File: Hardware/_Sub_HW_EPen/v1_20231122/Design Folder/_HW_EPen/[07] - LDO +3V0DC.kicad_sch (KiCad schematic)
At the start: 4 parts, among them U701 MIC5365-3.0YC5-TR

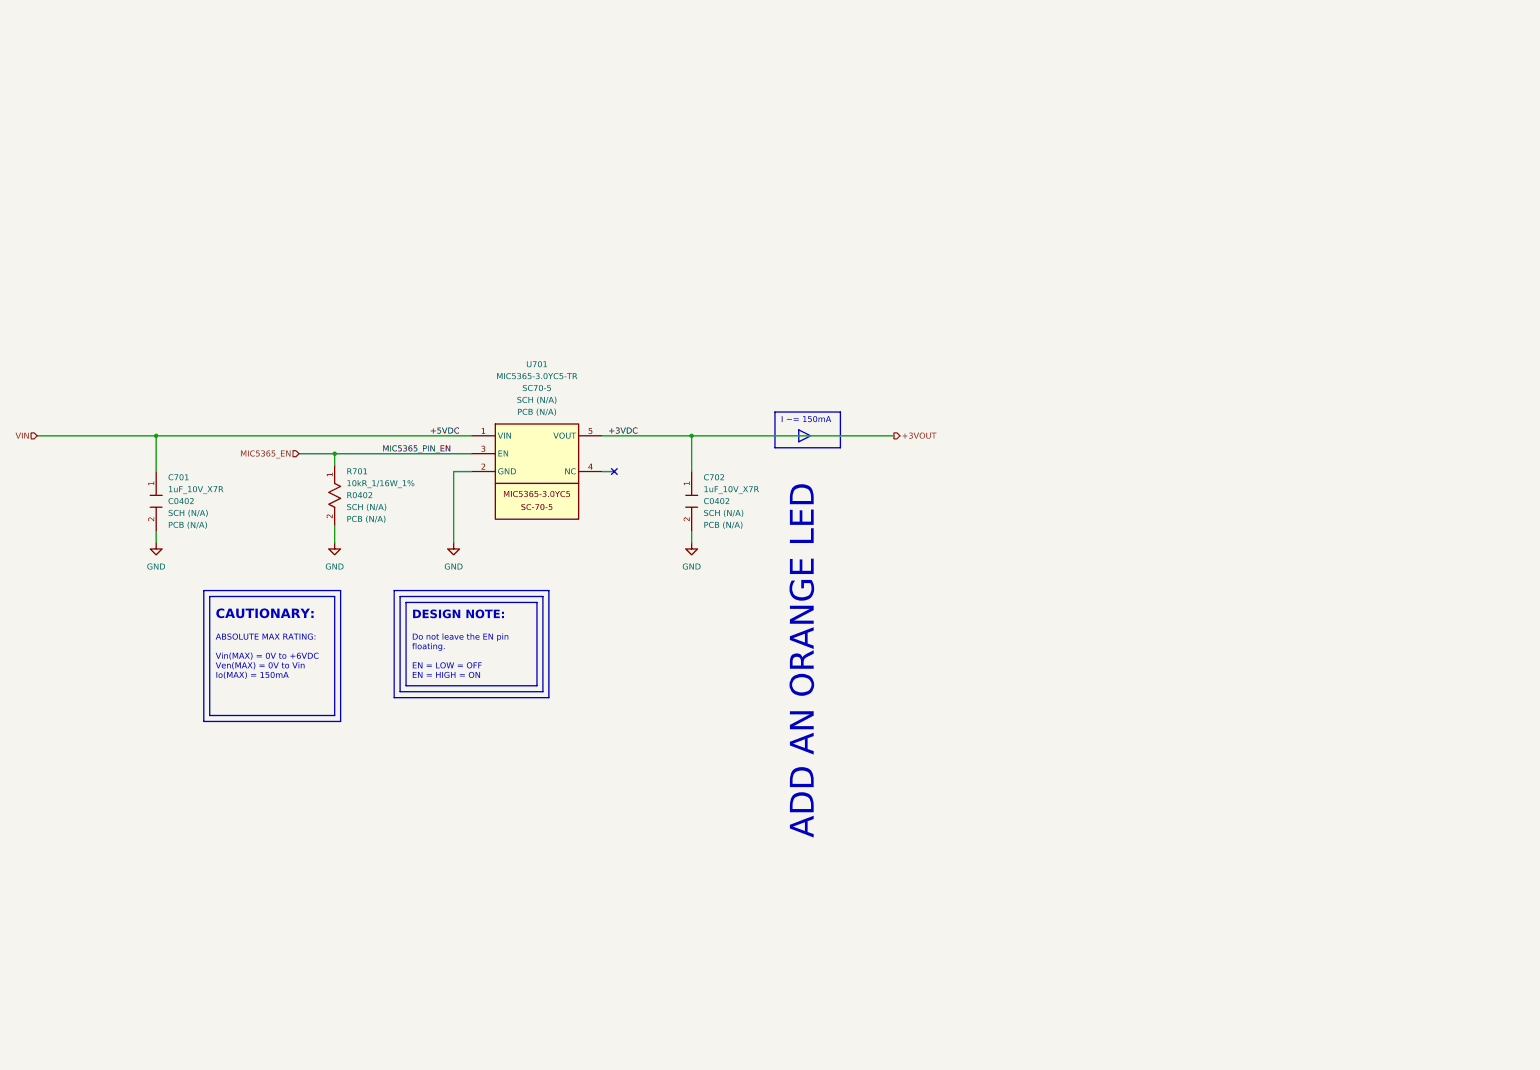
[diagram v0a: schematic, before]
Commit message: Working on EPen schematic
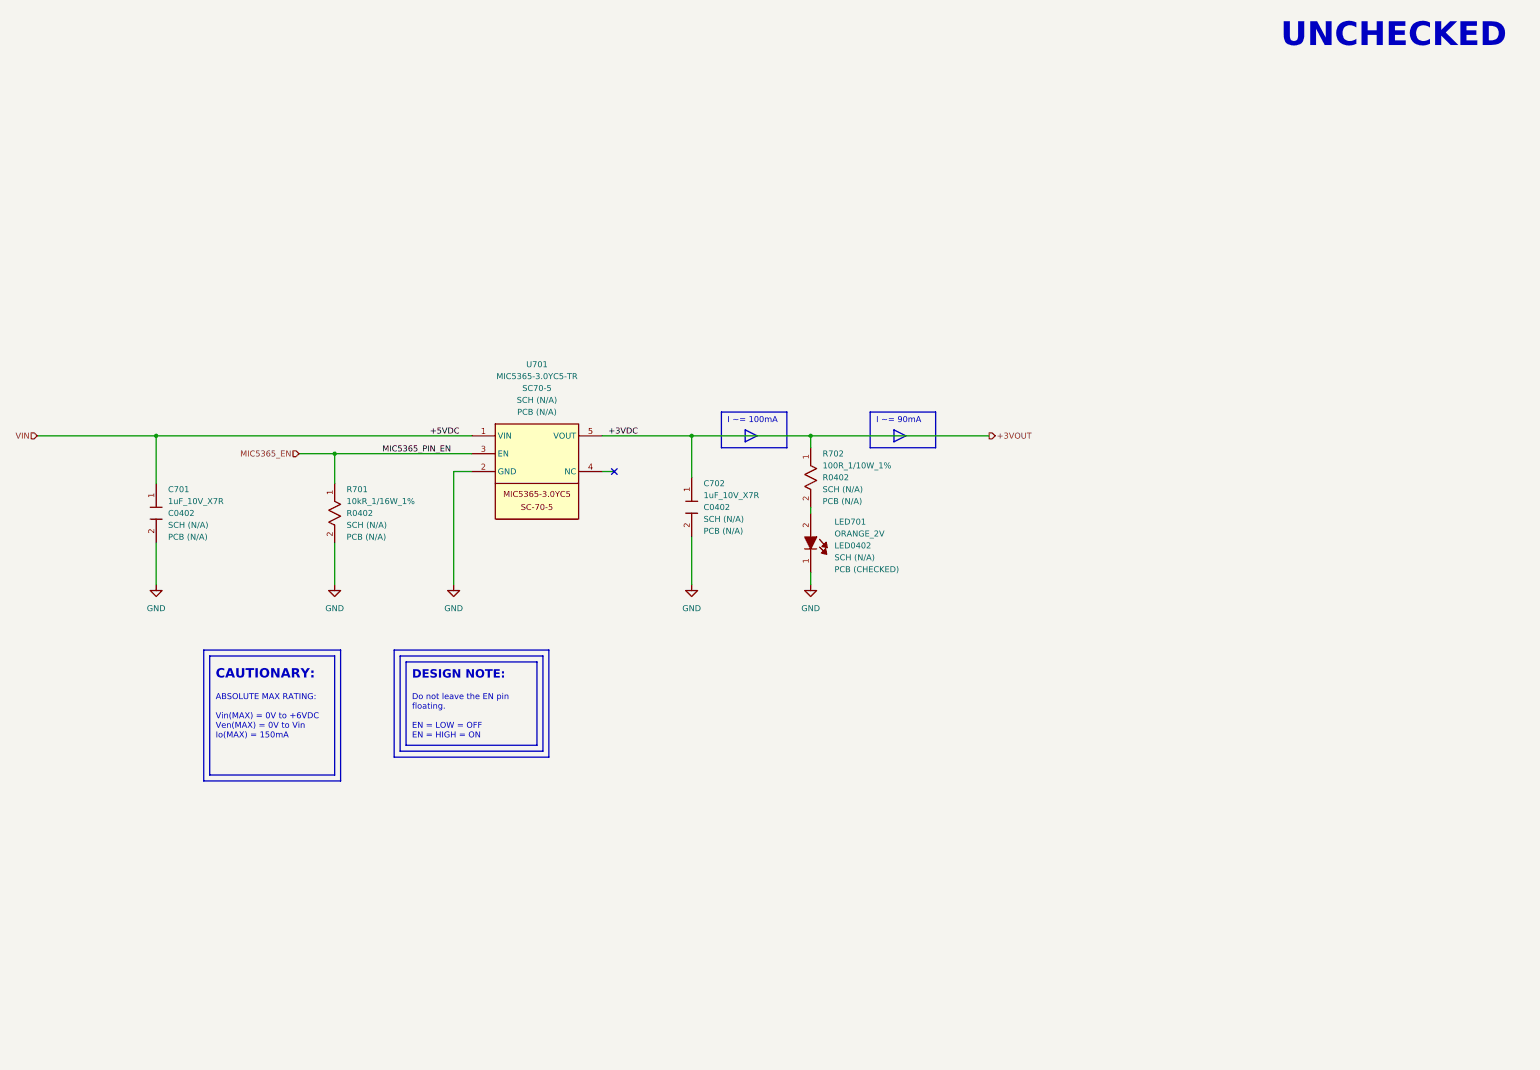
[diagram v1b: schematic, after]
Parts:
- added LED701: ORANGE_2V, LED_SMD:LED_0402_1005Metric, symbol _SCHLIB_EPen:LED_ORANGE_2V_605nm_LED0402
- added R702: 100R_1/10W_1%, Resistor_SMD:R_0402_1005Metric, symbol _SCHLIB_EPen:RES_100R_1/10W_1%_R0402
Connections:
- net +3VOUT: now also R702.1
- net GND: now also LED701.1
- new net: LED701.2, R702.2
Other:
- note added: "I ~= 100mA"
- note added: "I ~= 90mA"
- note added: "UNCHECKED"
- note removed: "ADD AN ORANGE LED"
- note removed: "I ~= 150mA"
- moved on the sheet: C701, C702, R701

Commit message: More progress on EPen Hardware
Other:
- note removed: "UNCHECKED"
- company: (none) -> mend0z0
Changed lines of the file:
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@@
 (kicad_sch (version 20230121) (generator eeschema)
   (paper "B")
+  (title_block
+    (company "mend0z0")
+    (comment 1 "v1.0")
+    (comment 2 "PRELIMINARY")
+    (comment 4 "_BOM_EPen.html")
+    (comment 5 "_HW_EPen.pcb")
+    (comment 6 "_GBR_EPen.zip")
+    (comment 7 "_BOM_EPen.html")
+    (comment 9 "First Release")
+  )
   (junction (at 127 119.38) (diameter 0) (color 0 0 0 0)
   )
@@
     (fill (type none))
   )
-  (text "UNCHECKED" (at 367.03 36.83 0)
-    (effects (font (size 5.08 5.08) (thickness 1.016) bold) (justify left bottom))
-  )
   (text "CAUTIONARY:" (at 139.7 171.45 0)

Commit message: _HW_EPen is ready to be worked for layout
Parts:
- C701, C702, LED701, R701, R702, U701: SCH CHECK SCH (N/A) -> SCH (CHECKED)
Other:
- note added: "Do not leave the EN pin floating. EN = LOW = OFF (default) EN = HIGH = ON"
- note removed: "Do not leave the EN pin floating. EN = LOW = OFF EN = HIGH = ON"
- title: (none) -> _HW_EPen
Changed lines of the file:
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@@
   (paper "B")
   (title_block
+    (title "_HW_EPen")
+    (date "2023-11-28")
+    (rev "v1.0")
     (company "mend0z0")
     (comment 1 "v1.0")
-    (comment 2 "PRELIMINARY")
+    (comment 2 "CHECKED")
     (comment 4 "_BOM_EPen.html")
     (comment 5 "_HW_EPen.pcb")
     (comment 6 "_GBR_EPen.zip")
     (comment 7 "_BOM_EPen.html")
+    (comment 8 "N/A")
     (comment 9 "First Release")
   )
@@
     (effects (font (size 1.27 1.27)) (justify left bottom))
   )
-  (text "Do not leave the EN pin\nfloating.\n\nEN = LOW = OFF\nEN = HIGH = ON"
+  (text "Do not leave the EN pin\nfloating.\n\nEN = LOW = OFF (default)\nEN = HIGH = ON"
     (at 181.61 184.15 0)
     (effects (font (size 1.27 1.27)) (justify left bottom))
@@
       (effects (font (size 1.27 1.27)) (justify left))
     )
-    (property "SCH CHECK" "SCH (N/A)" (at 129.54 138.43 90)
+    (property "SCH CHECK" "SCH (CHECKED)" (at 129.54 138.43 90)
       (effects (font (size 1.27 1.27)) (justify left))
     )
@@
       (effects (font (size 1.27 1.27)) (justify left))
     )
-    (property "SCH CHECK" "SCH (N/A)" (at 269.24 130.81 90)
+    (property "SCH CHECK" "SCH (CHECKED)" (at 269.24 130.81 90)
       (effects (font (size 1.27 1.27)) (justify left))
     )
@@
       (effects (font (size 1.27 1.27)) (justify left))
     )
-    (property "SCH CHECK" "SCH (N/A)" (at 167.64 138.43 90)
+    (property "SCH CHECK" "SCH (CHECKED)" (at 167.64 138.43 90)
       (effects (font (size 1.27 1.27)) (justify left))
     )
@@
       (effects (font (size 1.27 1.27)) (justify left))
     )
-    (property "SCH CHECK" "SCH (N/A)" (at 271.78 145.3515 90)
+    (property "SCH CHECK" "SCH (CHECKED)" (at 271.78 145.3515 90)
       (effects (font (size 1.27 1.27)) (justify left))
     )
@@
       (effects (font (size 1.27 1.27)) (justify left))
     )
-    (property "SCH CHECK" "SCH (N/A)" (at 243.84 137.16 90)
+    (property "SCH CHECK" "SCH (CHECKED)" (at 243.84 137.16 90)
       (effects (font (size 1.27 1.27)) (justify left))
     )
@@
       (effects (font (size 1.27 1.27)))
     )
-    (property "SCH CHECK" "SCH (N/A)" (at 208.28 111.76 0)
-      (effects (font (size 1.27 1.27)))
-    )
+    (property "SCH CHECK" "SCH (CHECKED)" (at 208.28 111.76 0)
+      (effects (font (size 1.27 1.27)))
+    )

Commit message: Updating file templates and structures...
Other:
- moved on the sheet: C701, C702, LED701, R701, R702, U701

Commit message: Updating Hardware File structures
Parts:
- C701, C702: Manufacturer (none) -> Murata Electronics; Part Number GRM155Z71A105KE01D -> (none); Part Number (Manufacturer) (none) -> GRM155Z71A105KE01D; Part Number (Vendor) (none) -> 490-GRM155Z71A105KE01DTR-ND; Vendor (none) -> Digikey
- LED701: Manufacturer (none) -> Harvatek Corporation; Part Number B2841UD--20D000614U1930 -> (none); Part Number (Manufacturer) (none) -> B2841UD--20D000614U1930; Part Number (Vendor) (none) -> 3147-B2841UD--20D000614U1930TR-ND; Vendor (none) -> Digikey
- R701: Manufacturer (none) -> Bourns Inc.; Part Number CR0402-FX-1002GLF -> (none); Part Number (Manufacturer) (none) -> CR0402-FX-1002GLF; Part Number (Vendor) (none) -> CR0402-FX-1002GLFTR-ND; Vendor (none) -> Digikey
- R702: Manufacturer (none) -> KOA Speer Electronics, Inc.; Part Number RK73H1ETTP1000F -> (none); Part Number (Manufacturer) (none) -> RK73H1ETTP1000F; Part Number (Vendor) (none) -> 2019-RK73H1ETTP1000FTR-ND; Vendor (none) -> Digikey
- U701: Manufacturer (none) -> Microchip Technology; Part Number MIC5365-3.0YC5-TR -> (none); Part Number (Manufacturer) (none) -> MIC5365-3.0YC5-TR; Part Number (Vendor) (none) -> 576-3191-2-ND; Vendor (none) -> Digikey
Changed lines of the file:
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@@
   (title_block
     (title "_HW_EPen")
-    (date "2023-11-28")
+    (date "2023/11/28")
     (rev "v1.0")
     (company "mend0z0")
     (comment 1 "v1.0")
     (comment 2 "CHECKED")
-    (comment 4 "_BOM_EPen.html")
-    (comment 5 "_HW_EPen.pcb")
+    (comment 3 "Siavash Taher Parvar")
+    (comment 4 "_BOM_EPen.csv")
+    (comment 5 "_HW_EPen.kicad_pcb")
     (comment 6 "_GBR_EPen.zip")
     (comment 7 "_BOM_EPen.html")
@@
       (effects (font (size 1.27 1.27)) (justify left) hide)
     )
-    (property "Part Number" "GRM155Z71A105KE01D" (at 220.98 191.77 0)
-      (effects (font (size 1.27 1.27)) (justify left) hide)
-    )
     (property "Link" "https://www.digikey.ca/en/products/detail/murata-electronics/GRM155Z71A105KE01D/13905035" (at 213.36 191.77 0)
       (effects (font (size 1.27 1.27)) (justify left) hide)
@@
       (effects (font (size 1.27 1.27)) (justify left))
     )
+    (property "Part Number (Vendor)" "490-GRM155Z71A105KE01DTR-ND" (at 201.93 189.23 0)
+      (effects (font (size 1.27 1.27)) hide)
+    )
+    (property "Part Number (Manufacturer)" "GRM155Z71A105KE01D" (at 223.52 191.77 0)
+      (effects (font (size 1.27 1.27)) (justify left) hide)
+    )
+    (property "Manufacturer" "Murata Electronics" (at 226.06 191.77 0)
+      (effects (font (size 1.27 1.27)) (justify left) hide)
+    )
+    (property "Vendor" "Digikey" (at 228.6 191.77 0)
+      (effects (font (size 1.27 1.27)) (justify left) hide)
+    )
     (pin "2")
     (pin "1")
@@
       (effects (font (size 1.27 1.27)) (justify left) hide)
     )
-    (property "Part Number" "RK73H1ETTP1000F" (at 360.68 184.15 0)
-      (effects (font (size 1.27 1.27)) (justify left) hide)
-    )
     (property "Link" "https://www.digikey.ca/en/products/detail/koa-speer-electronics-inc/RK73H1ETTP1000F/9844157" (at 353.06 184.15 0)
       (effects (font (size 1.27 1.27)) (justify left) hide)
@@
       (effects (font (size 1.27 1.27)) (justify left))
     )
+    (property "Part Number (Vendor)" "2019-RK73H1ETTP1000FTR-ND" (at 341.63 181.61 0)
+      (effects (font (size 1.27 1.27)) hide)
+    )
+    (property "Part Number (Manufacturer)" "RK73H1ETTP1000F" (at 363.22 184.15 0)
+      (effects (font (size 1.27 1.27)) (justify left) hide)
+    )
+    (property "Manufacturer" "KOA Speer Electronics, Inc." (at 365.76 184.15 0)
+      (effects (font (size 1.27 1.27)) (justify left) hide)
+    )
+    (property "Vendor" "Digikey" (at 368.3 184.15 0)
+      (effects (font (size 1.27 1.27)) (justify left) hide)
+    )
     (pin "1")
     (pin "2")
@@
       (effects (font (size 1.27 1.27)) (justify left) hide)
     )
-    (property "Part Number" "CR0402-FX-1002GLF" (at 259.08 191.77 0)
-      (effects (font (size 1.27 1.27)) (justify left) hide)
-    )
     (property "Link" "https://www.digikey.ca/en/products/detail/bourns-inc/CR0402-FX-1002GLF/3593192" (at 251.46 191.77 0)
       (effects (font (size 1.27 1.27)) (justify left) hide)
@@
       (effects (font (size 1.27 1.27)) (justify left))
     )
+    (property "Part Number (Vendor)" "CR0402-FX-1002GLFTR-ND" (at 240.03 189.23 0)
+      (effects (font (size 1.27 1.27)) hide)
+    )
+    (property "Part Number (Manufacturer)" "CR0402-FX-1002GLF" (at 261.62 191.77 0)
+      (effects (font (size 1.27 1.27)) (justify left) hide)
+    )
+    (property "Manufacturer" "Bourns Inc." (at 264.16 191.77 0)
+      (effects (font (size 1.27 1.27)) (justify left) hide)
+    )
+    (property "Vendor" "Digikey" (at 266.7 191.77 0)
+      (effects (font (size 1.27 1.27)) (justify left) hide)
+    )
     (pin "1")
     (pin "2")
@@
       (effects (font (size 1.27 1.27)) (justify left) hide)
     )
-    (property "Part Number" "B2841UD--20D000614U1930" (at 363.22 200.66 0)
-      (effects (font (size 1.27 1.27)) (justify left) hide)
-    )
     (property "Link" "https://www.digikey.ca/en/products/detail/harvatek-corporation/B2841UD-20D000614U1930/16729512" (at 355.6 200.66 0)
       (effects (font (size 1.27 1.27)) (justify left) hide)
@@
       (effects (font (size 1.27 1.27)) (justify left))
     )
+    (property "Part Number (Vendor)" "3147-B2841UD--20D000614U1930TR-ND" (at 341.63 195.58 0)
+      (effects (font (size 1.27 1.27)) hide)
+    )
+    (property "Part Number (Manufacturer)" "B2841UD--20D000614U1930" (at 365.76 200.66 0)
+      (effects (font (size 1.27 1.27)) (justify left) hide)
+    )
+    (property "Manufacturer" "Harvatek Corporation" (at 368.3 200.66 0)
+      (effects (font (size 1.27 1.27)) (justify left) hide)
+    )
+    (property "Vendor" "Digikey" (at 370.84 200.66 0)
+      (effects (font (size 1.27 1.27)) (justify left) hide)
+    )
     (pin "2")
     (pin "1")
@@
       (effects (font (size 1.27 1.27)) (justify left) hide)
     )
-    (property "Part Number" "GRM155Z71A105KE01D" (at 335.28 190.5 0)
-      (effects (font (size 1.27 1.27)) (justify left) hide)
-    )
     (property "Link" "https://www.digikey.ca/en/products/detail/murata-electronics/GRM155Z71A105KE01D/13905035" (at 327.66 190.5 0)
       (effects (font (size 1.27 1.27)) (justify left) hide)
@@
       (effects (font (size 1.27 1.27)) (justify left))
     )
+    (property "Part Number (Vendor)" "490-GRM155Z71A105KE01DTR-ND" (at 316.23 187.96 0)
+      (effects (font (size 1.27 1.27)) hide)
+    )
+    (property "Part Number (Manufacturer)" "GRM155Z71A105KE01D" (at 337.82 190.5 0)
+      (effects (font (size 1.27 1.27)) (justify left) hide)
+    )
+    (property "Manufacturer" "Murata Electronics" (at 340.36 190.5 0)
+      (effects (font (size 1.27 1.27)) (justify left) hide)
+    )
+    (property "Vendor" "Digikey" (at 342.9 190.5 0)
+      (effects (font (size 1.27 1.27)) (justify left) hide)
+    )
     (pin "2")
     (pin "1")
@@
       (effects (font (size 1.27 1.27)) (justify left) hide)
     )
-    (property "Part Number" "MIC5365-3.0YC5-TR" (at 276.86 157.48 0)
-      (effects (font (size 1.27 1.27)) (justify left) hide)
-    )
     (property "Link" "https://www.digikey.ca/en/products/detail/microchip-technology/MIC5365-3-0YC5-TR/1868092" (at 276.86 165.1 0)
       (effects (font (size 1.27 1.27)) (justify left) hide)
@@
       (effects (font (size 1.27 1.27)))
     )
-    (pin "1")
+    (property "Part Number (Vendor)" "576-3191-2-ND" (at 274.32 176.53 0)
+      (effects (font (size 1.27 1.27)) hide)
+    )
+    (property "Part Number (Manufacturer)" "MIC5365-3.0YC5-TR" (at 276.86 154.94 0)
+      (effects (font (size 1.27 1.27)) (justify left) hide)
+    )
+    (property "Manufacturer" "Microchip Technology" (at 276.86 152.4 0)
+      (effects (font (size 1.27 1.27)) (justify left) hide)
+    )
+    (property "Vendor" "Digikey" (at 276.86 149.86 0)
+      (effects (font (size 1.27 1.27)) (justify left) hide)
+    )
+    (pin "1")
